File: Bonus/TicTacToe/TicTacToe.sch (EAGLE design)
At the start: 61 parts

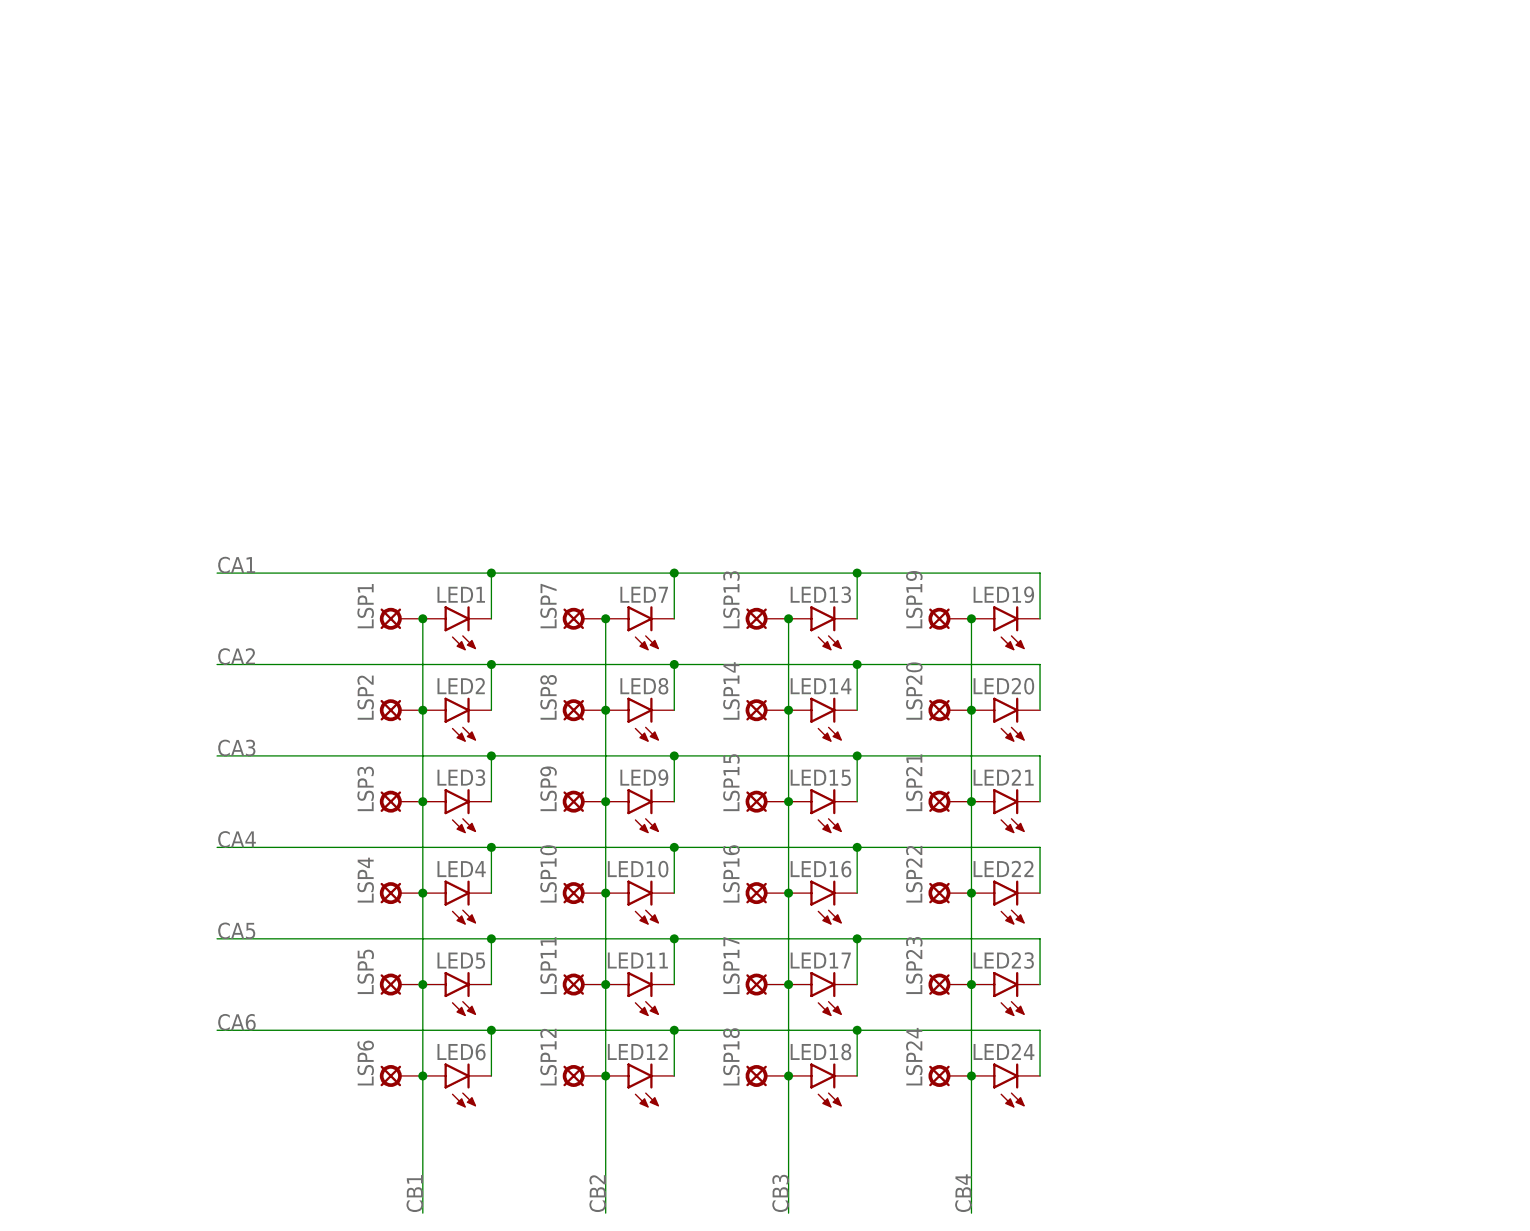
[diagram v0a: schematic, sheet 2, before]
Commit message: Restored original 2020 pendant in directory, made a new directory for 2021 fabbed pendant, and a directory for Bonus PCB.
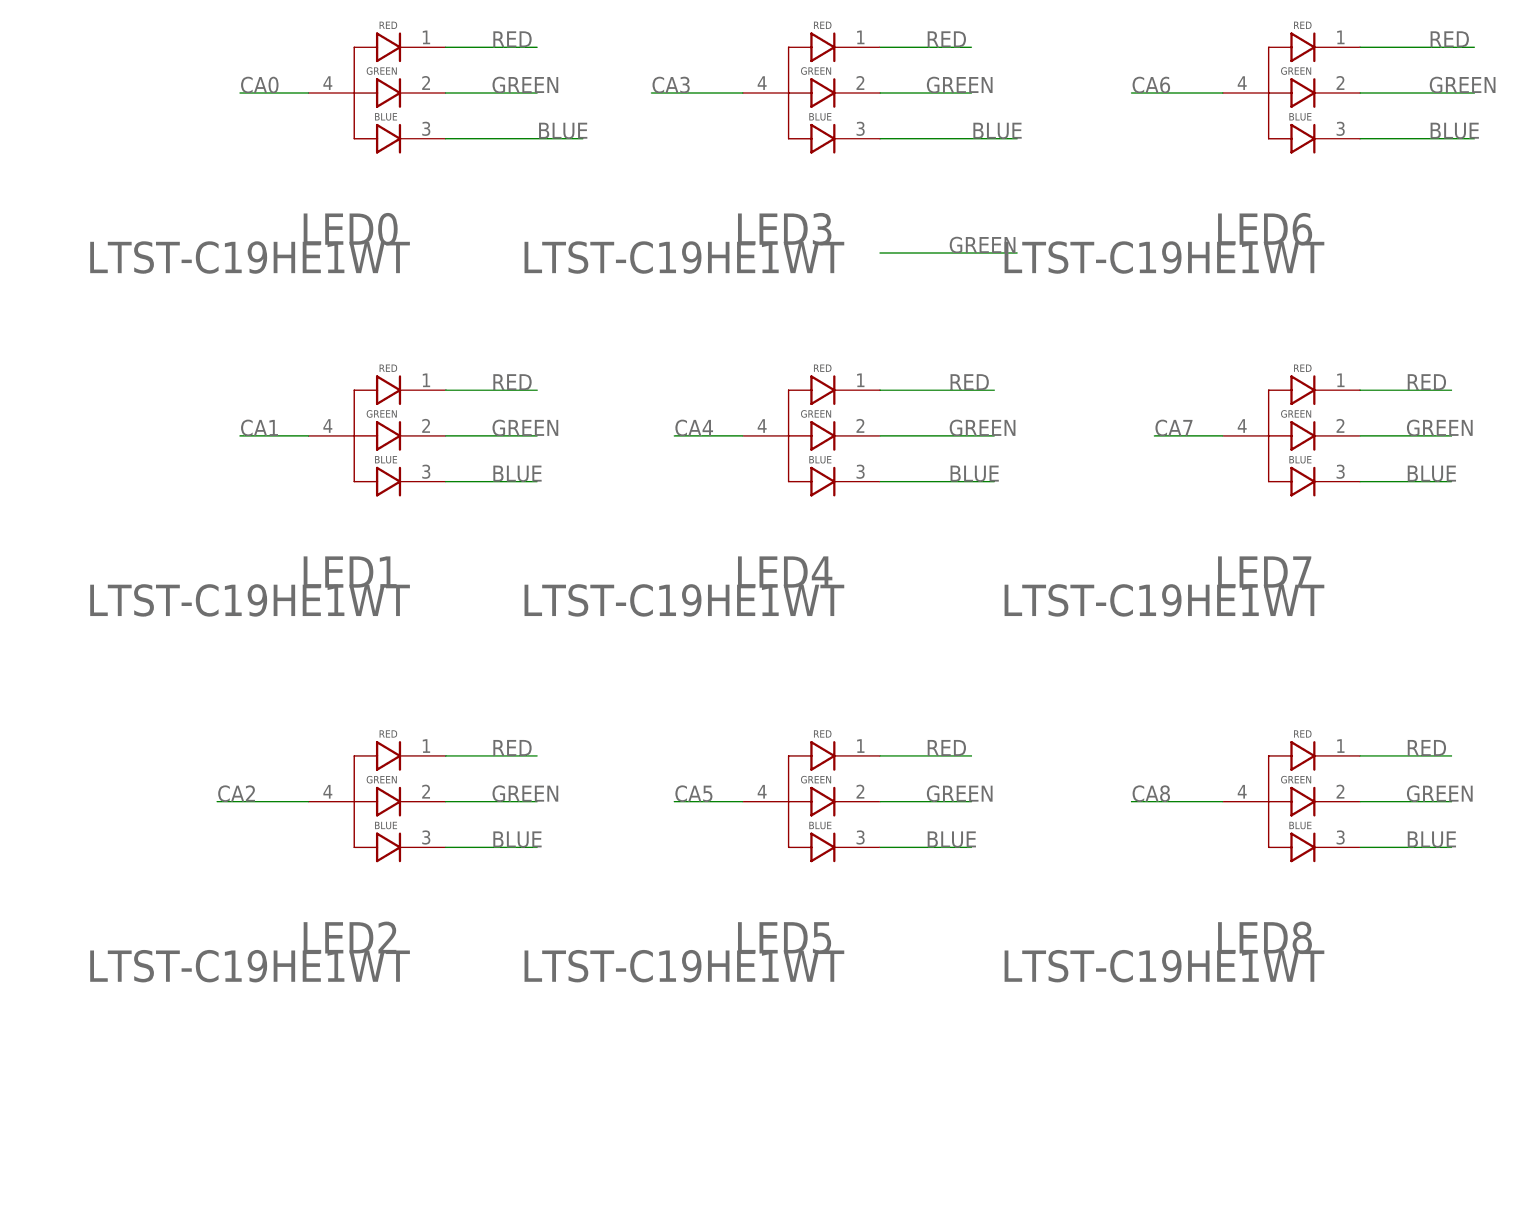
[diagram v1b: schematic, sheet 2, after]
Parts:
- removed LED10, LED11, LED12, LED13, LED14, LED15, LED16, LED17, LED18, LED19, LED20, LED21, LED22, LED23, LED24, LED9: (no value), led:LEDCHIPLED_1206
- removed LSP1, LSP10, LSP11, LSP12, LSP13, LSP14, LSP15, LSP16, LSP17, LSP18, LSP19, LSP2, LSP20, LSP21, LSP22, LSP23, LSP24, LSP3, LSP4, LSP5, LSP6, LSP7, LSP8, LSP9: LSP10, solpad-mod:LSP10
- removed R10, R5, R6: (no value), rcl:R-US_R1206
- added C3: 470nF, rcl:C-USC0805
- added LED0: LTST-C19HE1WT, LTST-C19HE1WT:LTST-C19HE1WT
- added S2: MOMENTARY-SWITCH-SPST-SMD-5.2MM, SparkFun-Switches-Modified:MOMENTARY-SWITCH-SPST-SMD-5.2MM
- BAT1: device Battery:BATTERYFOB -> 1060TR:1060TR
- C2: device rcl:C-USC1206 -> rcl:C-USC0805
- LED1, LED2, LED3, LED4, LED5, LED6, LED7, LED8: value (none) -> LTST-C19HE1WT; device led:LEDCHIPLED_1206 -> LTST-C19HE1WT:LTST-C19HE1WT
- R1, R2, R3, R4: device rcl:R-US_R1206 -> rcl:R-US_R0805
- S1: value MOMENTARY-SWITCH-SPST-PTH-6.0MM -> MOMENTARY-SWITCH-SPST-SMD-5.2MM; device SparkFun-Switches:MOMENTARY-SWITCH-SPST-PTH-6.0MM -> SparkFun-Switches-Modified:MOMENTARY-SWITCH-SPST-SMD-5.2MM
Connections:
- removed net CAP1: MSP430.19
- removed net CAP2: MSP430.18
- removed net CB1: LED1.A, LED2.A, LED3.A, LED4.A, LED5.A, LED6.A, LSP1.MP, LSP2.MP, LSP3.MP, LSP4.MP, LSP5.MP, LSP6.MP, MSP430.9
- removed net CB2: LED10.A, LED11.A, LED12.A, LED7.A, LED8.A, LED9.A, LSP10.MP, LSP11.MP, LSP12.MP, LSP7.MP, LSP8.MP, LSP9.MP, MSP430.10
- removed net CB3: LED13.A, LED14.A, LED15.A, LED16.A, LED17.A, LED18.A, LSP13.MP, LSP14.MP, LSP15.MP, LSP16.MP, LSP17.MP, LSP18.MP, MSP430.12
- removed net CB4: LED19.A, LED20.A, LED21.A, LED22.A, LED23.A, LED24.A, LSP19.MP, LSP20.MP, LSP21.MP, LSP22.MP, LSP23.MP, LSP24.MP, MSP430.13
- removed net N$3: MSP430.2, R1.1
- removed net N$4: MSP430.3, R2.1
- removed net N$5: MSP430.4, R3.1
- removed net N$6: MSP430.5, R4.1
- removed net N$7: MSP430.6, R5.1
- removed net N$8: MSP430.7, R6.1
- removed net N$9: MSP430.14
- removed net SWITCH1: C2.2, MSP430.15, S1.1
- new net BLUE: LED0.3, LED1.3, LED2.3, LED3.3, LED4.3, LED5.3, LED6.3, LED7.3, LED8.3, R1.2
- new net CA0: LED0.4, MSP430.2
- new net CA7: LED7.4, MSP430.15
- new net CA8: LED8.4, MSP430.8
- new net CB0: MSP430.19, R1.1
- new net GREEN: LED0.2, LED1.2, LED2.2, LED3.2, LED4.2, LED5.2, LED6.2, LED7.2, LED8.2, R2.2
- new net N$2: MSP430.13, R2.1
- new net RED: LED0.1, LED1.1, LED2.1, LED3.1, LED4.1, LED5.1, LED6.1, LED7.1, LED8.1, R3.2
- new net SW0: C2.2, MSP430.9, S1.1
- new net SW1: C3.2, MSP430.10, S2.1
- net CA1: now also LED1.4, MSP430.3; no longer LED1.C, LED13.C, LED19.C, LED7.C, R1.2
- net CA2: now also LED2.4, MSP430.4; no longer LED14.C, LED2.C, LED20.C, LED8.C, R2.2
- net CA3: now also LED3.4, MSP430.5; no longer LED15.C, LED21.C, LED3.C, LED9.C, R3.2
- net CA4: now also LED4.4, MSP430.6; no longer LED10.C, LED16.C, LED22.C, LED4.C, R4.2
- net CA5: now also LED5.4, MSP430.7; no longer LED11.C, LED17.C, LED23.C, LED5.C, R5.2
- net CA6: now also LED6.4, MSP430.14; no longer LED12.C, LED18.C, LED24.C, LED6.C, R6.2
- net GND: now also C3.1, S2.2
- net N$1: now also MSP430.12, R3.1; no longer MSP430.8
- net VDD: now also R4.1; no longer R10.1
- net _RST: now also R4.2; no longer R10.2
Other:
- moved on the sheet: C2, R1, R2, R3, R4, S1
